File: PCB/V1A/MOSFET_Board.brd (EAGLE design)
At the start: 230 x 120 mm, 261 parts, among them IC301 7805T, IC302 7805T, J302 FAN_MOLEX4PIN, J303 FAN_MOLEX4PIN, Q201 SIRC10DP, Q202 SIRC10DP, Q203 BC817, Q204 BC817, Q205 SIRC10DP, Q206 SIRC10DP, Q207 BC817, Q208 BC807, Q209 BC817, Q210 BC807, Q211 IXTK102N65X2, Q212 IXTK102N65X2, Q401 BC807, Q402 BC807, Q403 BC807, Q404 BC807, Q405 BC807, Q406 BC807, Q407 BC807, Q408 BC807, Q409 BC807, Q410 BC807, Q411 BC807, Q412 BC807, Q413 BC807, Q414 BC807, U201 AD420, U202 AD420, U203 LT1014I, U204 LT1014I, U205 AD620, U206 AD620, U207 AD620, U208 AD620, U209 LTC1865L, U210 LTC1865L, U301 MAX743, U302 LP2985-3.1, U303 LM50, U304 LM50, U305 AD620, U306 LTC1865L, U307 LTC1865L, U401 HCPL-063N, U402 HCPL-063N, U403 HCPL-063N, U404 HCPL-063N, U405 HCPL-063N, U406 HCPL-063N, U407 HCPL-063N, X301 GMSTBA4

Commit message: Removed abandoned PCB attempts
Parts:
- added C1: 220µ, rcl:E3,5-10
- added C328, C330: 0.1µ, passives:C1608
- added C329: 1µ, passives:CT3216
- added L303: 4µ7, inductor-coilcraft:MSS7341
- C205, C207: value 0.01µ -> 10n
- C206, C208, C405, C406, C407, C408, C420, C421, C422: value 0.01µ -> 10n; device passives:C3216 -> passives:C2012
- C225, C226, C227, C228: value 100p -> 470p
- C303, C325: device passives:C3216 -> passives:C1608
- C311: value 220µ -> 10µ; device rcl:E3,5-10 -> passives:CT6032
- C313: value 1µ -> 220µ; device passives:C3216 -> rcl:E3,5-10
- C314: value 10n -> 1µ; device passives:C2012 -> passives:C3216
- C315: value 4µ7 -> 470p; device passives:C3216 -> rcl:C075-032X103
- C316: value 0.1µ -> 10n; device passives:C3216 -> passives:C2012
- C317: value 0.1µ -> 4µ7
- C318, C319, C326: value 1µ -> 0.1µ; device passives:CT3216 -> passives:C1608
- C320: value 150n -> 0.1µ; device rcl:C050-030X075 -> passives:C1608
- C322: value 0.1µ -> 1µ; device passives:C3216 -> passives:CT3216
- C323: value 0.1µ -> 150n; device passives:C3216 -> rcl:C050-030X075
- C324: value 500p -> 1µ; device passives:C1608 -> passives:CT3216
- C327: value 0.1µ -> 470p; device passives:C3216 -> passives:C1608
- moved C320 340.6 mm to (145.5, 40.0), flipped to the bottom, turned to 90 degrees
- moved C316 304.7 mm to (-50.0, -10.0), turned to 0 degrees
- moved C317 288.7 mm to (-46.0, -13.5)
- moved C318 283.8 mm to (-17.0, -70.0), turned to 180 degrees
- moved C323 224.4 mm to (-7.00, -86.0)
- moved J303 210.4 mm to (105.0, -33.0)
- moved R303 142.9 mm to (-7.00, -82.0)
- moved C424 127.5 mm to (-68.0, -53.5), flipped to the bottom, turned to 180 degrees
- moved C427 124.8 mm to (-72.0, -53.5), flipped to the bottom
- moved R427 123.7 mm to (-72.0, -51.0), flipped to the bottom
- moved C418 115.2 mm to (-70.0, -56.0), turned to 180 degrees
- moved C421 114.8 mm to (-70.0, -53.0), turned to 180 degrees
- moved R424 114.8 mm to (-68.0, -51.0), flipped to the bottom, turned to 180 degrees
- moved R418 112.4 mm to (-68.5, -62.5), turned to 90 degrees
- moved R421 109.7 mm to (-71.5, -62.5), turned to 90 degrees
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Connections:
- new net N$60: C315.1, L303.1, PS301.1
- net +12V: now also C1.+
- net +15V: now also C312.+, C326.1; no longer C311.+, C323.1
- net +3V3: now also C317.1, C324.+, C325.1, C329.+, C330.1; no longer C315.1, C321.+, C322.1, C326.+, C327.1
- net +5V: now also C311.+, C319.1, C320.1, L303.2; no longer C316.1, C317.1, PS301.1
- net +5V_I: now also C315.2, C318.1
- net -15V: now also C313.-, C328.1; no longer C312.-, C325.1
- net DUT-: now also C323.2; no longer C320.2
- net GND: now also C1.-, C312.-, C313.+, C319.2, C320.2, C322.-, C324.-, C326.2, C328.2, C329.-, C330.2; no longer C312.+, C313.2, C315.2, C318.-, C319.-, C322.2, C323.2, C324.2, C326.-
- net GNDI: now also C318.2
- net N$10: now also C316.1; no longer C314.1
- net N$30: now also C327.1; no longer C324.1
- net N$61: now also C323.1; no longer C320.1
- net TEMP1: now also C321.+; no longer C318.+
- net TEMP2: now also C322.+; no longer C319.+
- net VREF1: now also C314.1; no longer C313.1
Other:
- board size 230 x 120 mm -> 230 x 130 mm

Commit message: Finalizing components & placement
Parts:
- removed R301: 0R, passives:R3216W
- removed U303, U304: LM50, ic:SOT23W
- removed X301: GMSTBA4, con-phoenix-762:GMSTBA4
- added C2: 4µ7, passives:C3216
- added J1, J2: (no value), mechanical:AMPHENOL-12-762_2
- added JP3: (no value), pinhead:2X03
- added SJ1: (no value), jumper:SJW
- C201, C202, C203, C204, C211, C212, C213, C214, C215, C216, C217, C218, C219, C220, C221, C222, C223, C224, C231, C232, C303, C308, C309, C318, C319, C320, C325, C326, C328, C330, C401, C402, C403, C404, C417, C418, C419: value 0.1µ -> 100n
- C209, C210, C229, C230, C324, C329: value 1µ -> 4µ7; device passives:CT3216 -> passives:C3216
- C301, C302: value 0.33µ -> 470n; device passives:C3216 -> passives:C1608
- C304, C321, C322: value 1µ -> 470n; device passives:CT3216 -> passives:C1608
- C310: value 22µ -> 47µ; device passives:CT6032 -> passives:CT7343
- C314: value 1µ -> 4µ7
- C405, C406, C407, C408, C420, C421, C422: device passives:C2012 -> passives:C1608
- R229, R230, R255, R256, R257, R258, R310: device passives:R2012W -> passives:R1608
- moved C321 158.4 mm to (-3.00, 3.00), turned to 0 degrees
- moved C319 157.7 mm to (3.50, 11.0)
- moved C323 152.5 mm to (108.2, 14.0), turned to 90 degrees
- moved C320 151.8 mm to (-3.50, 11.0)
- moved R303 144.4 mm to (108.2, 5.00), turned to 270 degrees
- moved C324 144.2 mm to (-7.00, -3.00), turned to 90 degrees
- moved C322 140.0 mm to (3.00, 3.00), turned to 180 degrees
- moved C325 138.5 mm to (-4.00, -3.00), turned to 90 degrees
- moved U306 131.0 mm to (0.00, -3.00), turned to 180 degrees
- moved MOV301 64.4 mm to (101.0, -23.0)
- moved C402 53.2 mm to (-68.0, -33.0), flipped to the bottom, turned to 0 degrees
- moved C410 53.2 mm to (-66.0, -30.5)
- moved C414 53.2 mm to (-70.0, -30.5)
- moved R410 53.2 mm to (-66.0, -28.0)
- moved R414 53.2 mm to (-70.0, -28.0)
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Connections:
- net +3V3: now also C229.1, C230.1, C324.1, C329.1, R410.2, R411.2, R415.2, R419.2; no longer C229.+, C230.+, C324.+, C329.+, R413.2, R426.2, R427.2
- net +5V: now also C2.1, C209.1, C210.1, JP3.3, JP3.4, R413.2, R426.2, R427.2; no longer C209.+, C210.+, R410.2, R411.2, R415.2, R419.2, U303.1, U304.1
- net CONV_C1: now also C415.1, R415.1, U403.6; no longer C411.1, R411.1, U403.7
- net CONV_C1_I: now also Q407.1; no longer Q403.1
- net CONV_C2: now also C416.1, R416.1, U404.6; no longer C415.1, R415.1, U403.6
- net CONV_C2_I: now also Q408.1; no longer Q407.1
- net CONV_TEMP: now also C411.1, R411.1, U403.7; no longer C410.1, R410.1, U402.7
- net CONV_TEMP_I: now also Q403.1; no longer Q402.1
- net CONV_V: now also C412.1, R412.1, U404.7; no longer C414.1, R414.1, U402.6
- net CONV_V_I: now also Q404.1; no longer Q406.1
- net DUT+: now also J1.2; no longer X301.2
- net DUT-: now also J2.1, SJ1.2; no longer R301.2, X301.3
- net FLT_DAC: now also Q411.1; no longer Q414.1
- net FLT_DAC_I: now also C425.1, R425.1, U407.7; no longer C428.1, R428.1, U407.6
- net GND: now also C2.2, C209.2, C210.2, C229.2, C230.2, C304.2, C321.2, C322.2, C324.2, C329.2, JP3.1, JP3.2, SJ1.1; no longer C209.-, C210.-, C229.-, C230.-, C304.-, C321.-, C322.-, C324.-, C329.-, R301.1, U303.3, U304.3
- net MISO: now also Q414.1; no longer Q411.1
- net MISO_I: now also C428.1, R428.1, U407.6; no longer C425.1, R425.1, U407.7
- net MOSI: now also C410.1, R410.1, U402.7; no longer C416.1, R416.1, U404.6
- net MOSI_I: now also Q402.1; no longer Q408.1
- net N$35: now also C304.1; no longer C304.+
- net SCK: now also C414.1, R414.1, U402.6; no longer C412.1, R412.1, U404.7
- net SCK_I: now also Q406.1; no longer Q404.1
- net TEMP1: now also C321.1, JP3.5; no longer C321.+, U303.2
- net TEMP2: now also C322.1, JP3.6; no longer C322.+, U304.2
- net VSENSE+: now also J1.1; no longer X301.1
- net VSENSE-: now also J2.2; no longer X301.4
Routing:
- net SCK: track 0.00 -> 198.0 mm
- net MOSI: track 0.00 -> 194.2 mm
- net LATCH_DAC: track 0.00 -> 151.0 mm
- net MISO: track 0.00 -> 134.5 mm
- net FLT_DAC: track 0.00 -> 107.8 mm
- net SDO_DAC1: track 0.00 -> 106.0 mm
- net CONV_V: track 0.00 -> 56.6 mm
- net VSENSE-: track 0.00 -> 54.5 mm
- net GNDI: track 0.00 -> 53.5 mm, vias 0 -> 22
- net GND: track 84.9 -> 133.6 mm, vias 17 -> 39
- net +5V: track 11.6 -> 57.0 mm, vias 1 -> 19
- net +5V_I: track 0.00 -> 26.3 mm, vias 0 -> 11
- net CLR_DAC2: track 0.00 -> 16.5 mm, vias 0 -> 1
- net CLR_DAC1: track 0.00 -> 16.5 mm, vias 0 -> 1
- net CONV_TEMP: track 0.00 -> 14.7 mm
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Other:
- outline, holes or cut-outs redrawn

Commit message: Cleaned DOCS
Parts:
- moved J302 35.4 mm to (90.0, -57.0)
- moved IC302 30.1 mm to (75.0, -27.0), flipped to the bottom, turned to 0 degrees
- moved C302 26.2 mm to (80.0, -37.0), turned to 90 degrees
- moved C315 26.0 mm to (-11.0, -50.0)
- moved C309 23.4 mm to (70.0, -37.0), turned to 90 degrees
- moved IC301 20.1 mm to (75.0, -50.0), flipped to the bottom, turned to 0 degrees
- moved C308 18.7 mm to (70.0, -60.0), turned to 90 degrees
- moved J303 18.0 mm to (105.0, -57.0)
- moved C301 17.0 mm to (80.0, -60.0), turned to 90 degrees
- moved C2 16.0 mm to (60.0, -40.0)
- moved C303 16.0 mm to (60.0, -37.5)
- moved C304 16.0 mm to (60.0, -42.5)
- moved C305 16.0 mm to (60.0, -35.0)
- moved C306 16.0 mm to (60.0, -49.0)
- moved C307 16.0 mm to (60.0, -45.0)
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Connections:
- net +5V_I: now also JP301.16
- net BYP_I: now also JP301.8
- net CLR_DAC1_I: now also JP301.6
- net CLR_DAC2_I: now also JP301.5
- net CONV_C1_I: now also JP301.9
- net CONV_C2_I: now also JP301.11
- net CONV_TEMP_I: now also JP301.10
- net CONV_V_I: now also JP301.12
- net FAN1_PWM_I: now also JP301.14
- net FAN2_PWM_I: now also JP301.13
- net FLT_DAC_I: now also JP301.1
- net GNDI: now also JP301.15
- net LATCH_DAC_I: now also JP301.7
- net MISO_I: now also JP301.2
- net MOSI_I: now also JP301.4
- net SCK_I: now also JP301.3
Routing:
- net FAN1_PWM_I: track 0.00 -> 19.6 mm
- net FAN2_PWM_I: track 0.00 -> 17.6 mm
- net CONV_V_I: track 0.00 -> 15.6 mm
- net MISO_I: track 14.7 -> 28.6 mm
- net CONV_C2_I: track 0.00 -> 13.6 mm
- net SCK_I: track 0.00 -> 12.8 mm
- net FLT_DAC_I: track 14.7 -> 27.3 mm
- net CONV_TEMP_I: track 0.00 -> 11.7 mm
- net MOSI_I: track 0.00 -> 10.2 mm
- net CONV_C1_I: track 0.00 -> 9.97 mm
- net CLR_DAC2_I: track 0.00 -> 9.38 mm
- net BYP_I: track 0.00 -> 9.16 mm
- net CLR_DAC1_I: track 0.00 -> 8.57 mm
- net LATCH_DAC_I: track 0.00 -> 8.34 mm
- net +5V_I: track 26.3 -> 30.1 mm
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- added copper zone on layer 1, net +12V
- added copper zone on layer 2, net +5V_I
- added copper zone on layer 16, net GND
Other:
- board size 230 x 130 mm -> 230 x 115 mm
- board text added: "+5V"
- board text added: "BYP"
- board text added: "CLR1"
- board text added: "CLR2"
- board text added: "C_C1"
- board text added: "C_C2"
- board text added: "C_TEMP"
- board text added: "C_V"
- board text added: "FAN1"
- board text added: "FAN2"
- board text added: "FLT"
- board text added: "GND"
- board text added: "LATCH"
- board text added: "MISO"
- board text added: "MOSI"
- board text added: "SCK"

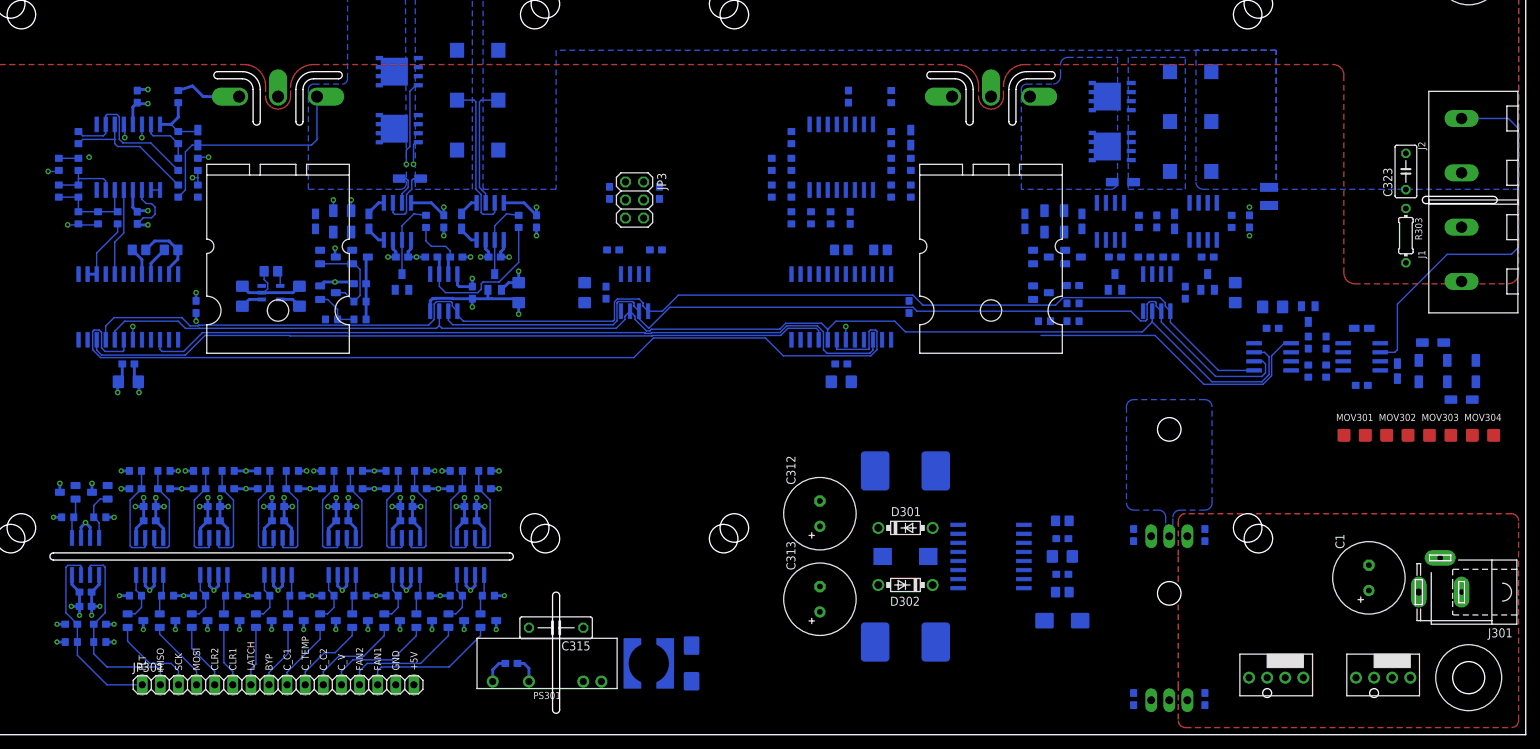
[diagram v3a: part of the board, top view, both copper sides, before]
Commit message: PCB layout & simulation
Added capacitance multiplier to +/-15V rails
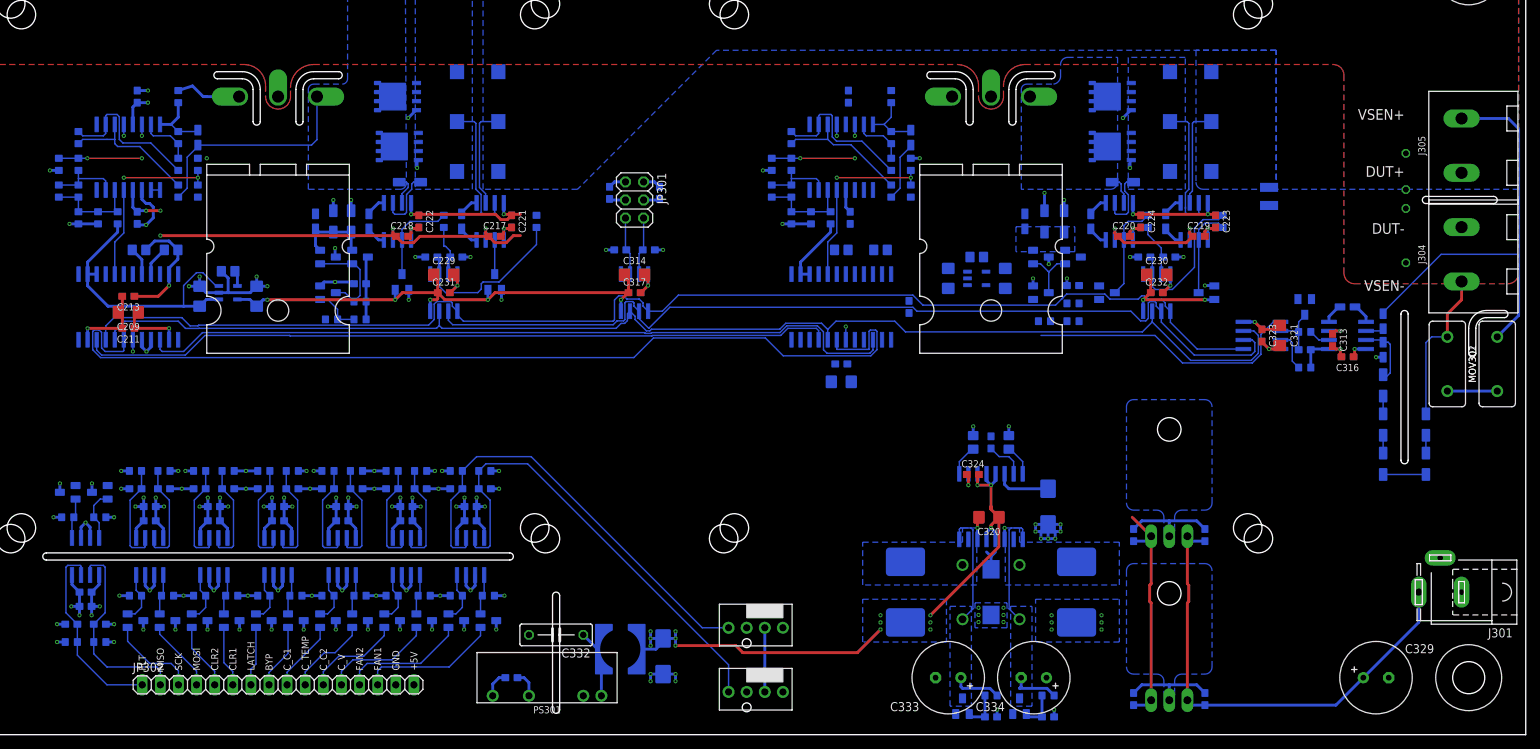
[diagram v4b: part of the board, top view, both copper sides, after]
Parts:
- removed C1: 220µ, rcl:E3,5-10
- removed C2: 4µ7, passives:C3216
- removed JP3: (no value), pinhead:2X03
- removed MOV303, MOV304: 180V, passives:R3225W
- removed U307: LTC1865L, ic:SO8
- added C331: 150n, rcl:C050-030X075
- added C332: 470p, rcl:C075-032X103
- added C333, C334: 220µ, rcl:E3,5-10
- added C335: 100n, passives:C1608
- added C336, C337: 470n, passives:C1608
- added JP302: CTRL, pinhead:1X16
- added Q301, Q302: BC817, transistors:SOT23
- added R301: 2M, passives:R3216W
- added R312, R313: 350R, passives:R1608
- added U303: AD620, ic:SO8
- added U304: LTC1865L, ic:SO8
- C301, C302, C321: value 470n -> 4µ7; device passives:C1608 -> passives:C3216
- C304: value 470n -> 10n; device passives:C1608 -> passives:C2012
- C306: value 10µ -> 4µ7; device passives:CT6032 -> passives:C3216
- C307: value 10n -> 4µ7; device passives:C2012 -> passives:C3216
- C308, C309, C325: value 100n -> 470n
- C310: value 47µ -> 470n; device passives:CT7343 -> passives:C1608
- C311: value 10µ -> 100n; device passives:CT6032 -> passives:C1608
- C312: value 220µ -> 470n; device rcl:E3,5-10 -> passives:C1608
- C313: value 220µ -> 100n; device rcl:E3,5-10 -> passives:C1608
- C315: device rcl:C075-032X103 -> passives:C1608
- C316: value 10n -> 100n; device passives:C2012 -> passives:C1608
- C317, C324: value 4µ7 -> 100n; device passives:C3216 -> passives:C1608
- C320: value 100n -> 4µ7; device passives:C1608 -> passives:C3216
- C322: value 470n -> 47µ; device passives:C1608 -> passives:CT7343
- C323: value 150n -> 100n; device rcl:C050-030X075 -> passives:C1608
- C326, C328: value 100n -> 10n; device passives:C1608 -> passives:C2012
- C327: value 470p -> 10µ; device passives:C1608 -> passives:CT6032
- C329: value 4µ7 -> 220µ; device passives:C3216 -> rcl:E3,5-10
- C330: value 100n -> 10µ; device passives:C1608 -> passives:CT6032
- D301: value 1N5817-B -> BAT54S; device diode:DO41-7.6 -> diode:SOT23
- D303: value BAT54S -> 1N5817-B; device diode:SOT23 -> diode:DO41-7.6
- J301: value (none) -> +12V
- J304: value (none) -> DUT+
- J305: value (none) -> DUT-
- JP301: value (none) -> TEMP; device pinhead:1X16 -> pinhead:2X03
- L302: value 100µ -> 4µ7; device passives:MSS1260 -> inductor-coilcraft:MSS7341
- L303: value 4µ7 -> 100µ; device inductor-coilcraft:MSS7341 -> passives:MSS1260
- MOV301, MOV302: value 180V -> 416NR10D; device passives:R3225W -> passives:DISK_9.5MM
- R302, R307: value 2M -> 2k15; device passives:R3216W -> passives:R2012W
- R303: value 16R -> 2M; device rcl:0204/7 -> passives:R3216W
- R309: value 2k15 -> 100R; device passives:R2012W -> passives:R1608
- R310: value 100R -> 10k
- R311: value 10k -> 16R; device passives:R1608 -> rcl:0204/7
- SJ301: value (none) -> DUT_GND
- U301: value MAX743 -> LP2985-3.1; device ic:SO16W -> ic:SOT23-5L
- U305: value AD620 -> LTC1865L
- U306: value LTC1865L -> MAX743; device ic:SO8 -> ic:SO16W
- moved C301 151.9 mm to (-61.0, -3.50)
- moved C316 151.5 mm to (100.0, -12.0), flipped to the top, turned to 180 degrees
- moved C304 124.5 mm to (-57.0, 0.00), turned to 0 degrees
- moved C306 121.8 mm to (-53.0, -3.50), turned to 90 degrees
- moved U301 113.2 mm to (-57.0, -3.00), turned to 90 degrees
- moved C315 112.0 mm to (94.0, -11.0), flipped to the bottom
- moved U302 99.0 mm to (48.0, -1.00)
- moved C330 97.1 mm to (4.00, -54.0), turned to 270 degrees
- moved C308 95.7 mm to (-2.00, 3.00), turned to 0 degrees
- moved C321 94.3 mm to (90.5, -9.00), flipped to the top, turned to 270 degrees
- moved J303 88.3 mm to (17.0, -50.0)
- moved C318 87.4 mm to (70.0, -60.0), turned to 90 degrees
- moved JP301 84.4 mm to (0.00, 10.0), turned to 270 degrees
- moved C319 82.0 mm to (70.0, -37.0)
- moved C313 80.6 mm to (97.9, -9.63), turned to 270 degrees
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- renumbered J1 to J304, J2 to J305, SJ1 to SJ301
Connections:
- new net +3V_1: C229.1, C231.1, C306.1, C314.1, C317.1, D201.2, D202.2, U209.8, U301.5, U304.8
- new net +3V_2: C230.1, C232.1, C307.1, C321.1, C323.1, D203.2, D204.2, D301.2, U210.8, U302.5, U305.8
- new net N$62: C305.1, U302.4
- new net N$63: C336.1, Q301.1, R312.2
- new net N$64: C334.-, D303.A, Q302.3, R313.1, U306.9
- new net N$65: C337.1, Q302.1, R313.2
- net +12V: now also C309.1, C310.1, C329.+; no longer C1.+, C301.1, C302.1
- net +15V: now also C313.1, Q301.2, U303.7; no longer C312.+, C326.1, D301.C, U301.16, U305.7
- net +3V3: no longer C229.1, C230.1, C231.1, C232.1, C317.1, C324.1, C325.1, C329.1, C330.1, D201.2, D202.2, D203.2, D204.2, D303.2, U209.8, U210.8, U302.5, U306.8, U307.8
- net +5V: now also C303.1, C311.1, C318.1, C322.+, C324.2, C330.+, JP301.3, JP301.4, L302.2, L303.1, U306.12, U306.13, U306.3, U306.4, U306.5; no longer C2.1, C303.2, C308.1, C309.1, C310.+, C311.+, JP3.3, JP3.4, L302.1, L303.2, U301.12, U301.13, U301.3, U301.4, U301.5
- net +5V_I: now also C332.2, C335.1, JP302.16; no longer C315.2, C318.1, JP301.16
- net -15V: now also C316.1, Q302.2, U303.4; no longer C313.-, C328.1, D302.A, U301.9, U305.4
- net BYP_I: now also JP302.8; no longer JP301.8
- net CLR_DAC1_I: now also JP302.6; no longer JP301.6
- net CLR_DAC2_I: now also JP302.5; no longer JP301.5
- net CONV_C1_I: now also JP302.9; no longer JP301.9
- net CONV_C2_I: now also JP302.11; no longer JP301.11
- net CONV_TEMP: now also U304.1; no longer U306.1
- net CONV_TEMP_I: now also JP302.10; no longer JP301.10
- net CONV_V: now also U305.1; no longer U307.1
- net CONV_V_I: now also JP302.12; no longer JP301.12
- net CSEN_L1: now also Q201.6, Q201.7, Q201.8, Q205.6, Q205.7, Q205.8
- net CSEN_L2: now also Q202.6, Q202.7, Q202.8, Q206.6, Q206.7, Q206.8
- net DUT+: now also R311.2; no longer R303.2
- net DUT-: now also C331.2; no longer C323.2
- net FAN1_PWM_I: now also JP302.14; no longer JP301.14
- net FAN2_PWM_I: now also JP302.13; no longer JP301.13
- net FLT_DAC_I: now also JP302.1; no longer JP301.1
- net GND: now also C303.2, C305.2, C306.2, C310.2, C311.2, C312.2, C313.2, C315.2, C318.2, C322.-, C323.2, C324.1, C326.1, C327.-, C329.-, C330.-, C333.-, C334.+, C336.2, C337.2, D301.1, JP301.1, JP301.2, R307.1, R310.1, U303.5, U304.4, U305.4, U306.11, U306.14, U306.2; no longer C1.-, C2.2, C303.1, C305.1, C306.-, C310.-, C311.-, C312.-, C313.+, C322.2, C324.2, C326.2, C327.2, C329.2, C330.2, D303.1, JP3.1, JP3.2, R308.1, R311.1, U301.11, U301.14, U305.5, U306.4, U307.4
- net GNDI: now also C335.2, JP302.15; no longer C318.2, JP301.15
- net LATCH_DAC_I: now also JP302.7; no longer JP301.7
- net MISO: now also U304.6, U305.6; no longer U306.6, U307.6
- net MISO_I: now also JP302.2; no longer JP301.2
- net MOSI: now also U304.5, U305.5; no longer U306.5, U307.5
- net MOSI_I: now also JP302.4; no longer JP301.4
- net N$10: now also C304.1, U301.4; no longer C316.1, U302.4
- net N$23: now also R309.1, U303.6; no longer R310.1, U305.6
- net N$24: now also R305.1, R306.2; no longer R306.1, R307.2
- net N$26: now also R303.2, R305.2; no longer R304.2, R306.2
- net N$27: now also R303.1, R304.2; no longer R304.1, R305.2
- net N$29: now also R306.1, R307.2, U303.3; no longer R307.1, R308.2, U305.3
- net N$30: now also C315.1, D301.3, R309.2, U305.2; no longer C327.1, D303.3, R310.2, U307.2
- net N$32: now also C333.+, D302.C, Q301.3, R312.1, U306.16; no longer MOV302.2, MOV303.1
- net N$33: now also R301.2, R304.1; no longer R302.2, R305.1
- net N$34: now also C328.1, U306.8; no longer C307.1, U301.8
- net N$35: now also C325.1, U306.7; no longer C304.1, U301.7
- net N$36: now also R302.2, U303.2; no longer MOV303.2, MOV304.1
- net N$37: now also C326.2, U306.1; no longer C305.2, U301.1
- net N$38: now also D302.A, L303.2, U306.15; no longer D301.A, L302.2, U301.15
- net N$39: now also D303.C, U306.10; no longer D302.C, U301.10
- net N$45: now also R310.2, U305.3; no longer R311.2, U307.3
- net N$60: now also C332.1, L302.1; no longer C315.1, L303.1
- net N$61: now also C331.1, R311.1; no longer C323.1, R303.1
- net RG1_H6: now also R308.2, U303.1; no longer R309.2, U305.1
- net RG2_H6: now also R308.1, U303.8; no longer R309.1, U305.8
- net SCK: now also U304.7, U305.7; no longer U306.7, U307.7
- net SCK_I: now also JP302.3; no longer JP301.3
- net TEMP1: now also C308.1, JP301.5, U304.2; no longer C321.1, JP3.5, U306.2
- net TEMP2: now also C312.1, JP301.6, U304.3; no longer C322.1, JP3.6, U306.3
- net VREF1: now also C301.1, U301.1, U301.3; no longer C314.1, U302.1, U302.3
- net VREF2: now also C302.1, U302.1, U302.3
- net VREF_MAX743: now also C327.+, U306.6; no longer C306.+, U301.6
- net VSENSE+: now also R301.1; no longer R302.1
- net VSENSE-: now also MOV302.2, R302.1; no longer MOV304.2, U305.2
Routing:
- net +5V: track 57.0 -> 178.9 mm, vias 19 -> 34
- net GND: track 133.6 -> 253.3 mm, vias 39 -> 90
- net +12V: track 19.5 -> 102.1 mm
- net +15V: track 12.3 -> 89.5 mm, vias 3 -> 8
- net +3V_1: track 0.00 -> 71.8 mm, vias 0 -> 5
- net FAN1_PWM: track 14.7 -> 65.6 mm
- net FAN2_PWM: track 14.7 -> 62.8 mm
- net VREF1: track 12.6 -> 41.1 mm
- net CSEN_H2: track 0.00 -> 28.3 mm
- net -15V: track 17.8 -> 43.0 mm, vias 4 -> 6
- net N$64: track 0.00 -> 23.5 mm
- net N$32: track 0.00 -> 23.5 mm
- net BYP2G1: track 0.00 -> 23.0 mm, vias 0 -> 2
- net N$44: track 0.00 -> 21.9 mm
- net VSENSE+: track 0.00 -> 21.9 mm
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- added copper zone on layer 16, net +5V
- added copper zone on layer 16, net BYP2
- added copper zone on layer 16, net N$32
- added copper zone on layer 16, net N$38
- added copper zone on layer 16, net N$39
- added copper zone on layer 16, net N$64
- removed copper zone on layer 1, net +12V
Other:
- outline, holes or cut-outs redrawn
- board text added: "DUT+"
- board text added: "DUT-"
- board text added: "VSEN+"
- board text added: "VSEN-"
